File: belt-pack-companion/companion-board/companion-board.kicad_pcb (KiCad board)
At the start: 4 copper layers, 29.4 x 47.2 mm, 58 parts, among them J1 Conn_01x18_Socket, J2 Conn_01x18_Socket, J4 Conn_01x03_Pin, U1 TLV320AIC3204, X1 YC24.576MUBCE2O

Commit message: Routing Progress
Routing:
- net LED_Red: track 0.00 -> 32.5 mm, vias 0 -> 1
- net SD_DETECT: track 1.31 -> 29.5 mm, vias 0 -> 1
- net Button_1: track 0.00 -> 24.5 mm, vias 0 -> 1
- net Net-(U1-IN2_R): track 0.00 -> 23.0 mm, vias 0 -> 2
- net Net-(U1-IN2_L): track 0.00 -> 22.4 mm, vias 0 -> 2
- net Button_2: track 0.00 -> 19.9 mm, vias 0 -> 1
- net LINE_IN_L: track 0.00 -> 4.88 mm
- net Net-(D1-Pad2): track 0.00 -> 1.18 mm
- net +3.3V: track 32.7 -> 33.8 mm, vias 9 -> 11
- net GND: vias 5 -> 6

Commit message: Routing complete
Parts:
- moved JP4 2.37 mm to (133.3, 73.4), turned to 0 degrees
- moved C1 0.06 mm to (129.2, 60.0)
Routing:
- net SD_DAT0: track 1.32 -> 37.7 mm, vias 0 -> 4
- net SD_DAT1: track 1.32 -> 37.7 mm, vias 0 -> 3
- net SD_CMD: track 1.32 -> 35.0 mm, vias 0 -> 2
- net MIC: track 18.1 -> 42.5 mm, vias 1 -> 2
- net SD_CLK: track 0.00 -> 21.6 mm, vias 0 -> 1
- net CODEC_RESET: track 1.07 -> 21.7 mm, vias 0 -> 1
- net I^{2}S_SPK_DATA: track 0.00 -> 18.7 mm, vias 0 -> 2
- net I^{2}S_WCLK: track 0.00 -> 18.4 mm, vias 0 -> 1
- net Button_PTT: track 1.52 -> 17.4 mm
- net I^{2}S_BCLK: track 0.00 -> 14.8 mm, vias 0 -> 1
- net I^{2}S_MIC_DATA: track 0.00 -> 14.4 mm
- net SD_DAT2: track 1.31 -> 13.4 mm, vias 0 -> 1
- net SD_DAT3: track 1.31 -> 13.3 mm
- net GND: track 7.30 -> 16.5 mm, vias 6 -> 37
- net LINE_IN_L: track 4.88 -> 12.4 mm
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
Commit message: Theoretically Finished Rev.1 of companion board
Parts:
- moved JP3 2.38 mm to (127.8, 71.5)
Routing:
- net GND: track 16.5 -> 19.6 mm, vias 37 -> 40
- net Net-(JP3-A): track 1.83 -> 3.72 mm
- net I^{2}S_SPK_DATA: track 18.7 -> 19.6 mm

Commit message: Incremented revision number to 1.1
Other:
- board text added: "Heltec WiFi LoRa 32 v3 Companion Board Rev 1.1"
- board text added: "Heltec v3 Companion Rev 1.1"
- board text removed: "Heltec WiFi LoRa 32 v3 Companion Board Rev.1"
- board text removed: "Heltec v3 Companion Rev.1"
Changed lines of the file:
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@@
 		)
 	)
-	(gr_text "Heltec v3\nCompanion\nRev.1"
+	(gr_text "Heltec v3\nCompanion\nRev 1.1"
 		(at 134.3 82.55 90)
 		(layer "F.SilkS")
@@
 		)
 	)
-	(gr_text "Heltec WiFi LoRa 32 v3\nCompanion Board\nRev.1"
+	(gr_text "Heltec WiFi LoRa 32 v3\nCompanion Board\nRev 1.1"
 		(at 123.318262 81.009202 0)
 		(layer "B.SilkS")
@@
 	)
 	(segment
-		(start 122.55 79.9076)
+		(start 121.65 79.9076)
 		(end 126.37627 79.9076)
 		(width 0.2)
@@
 	)
 	(via
-		(at 122.55 79.9076)
+		(at 121.65 79.9076)
 		(size 0.6)
 		(drill 0.3)
@@
 	)
 	(segment
-		(start 122.55 79.9076)
+		(start 121.65 79.9076)
 		(end 114.1604 79.9076)
 		(width 0.2)

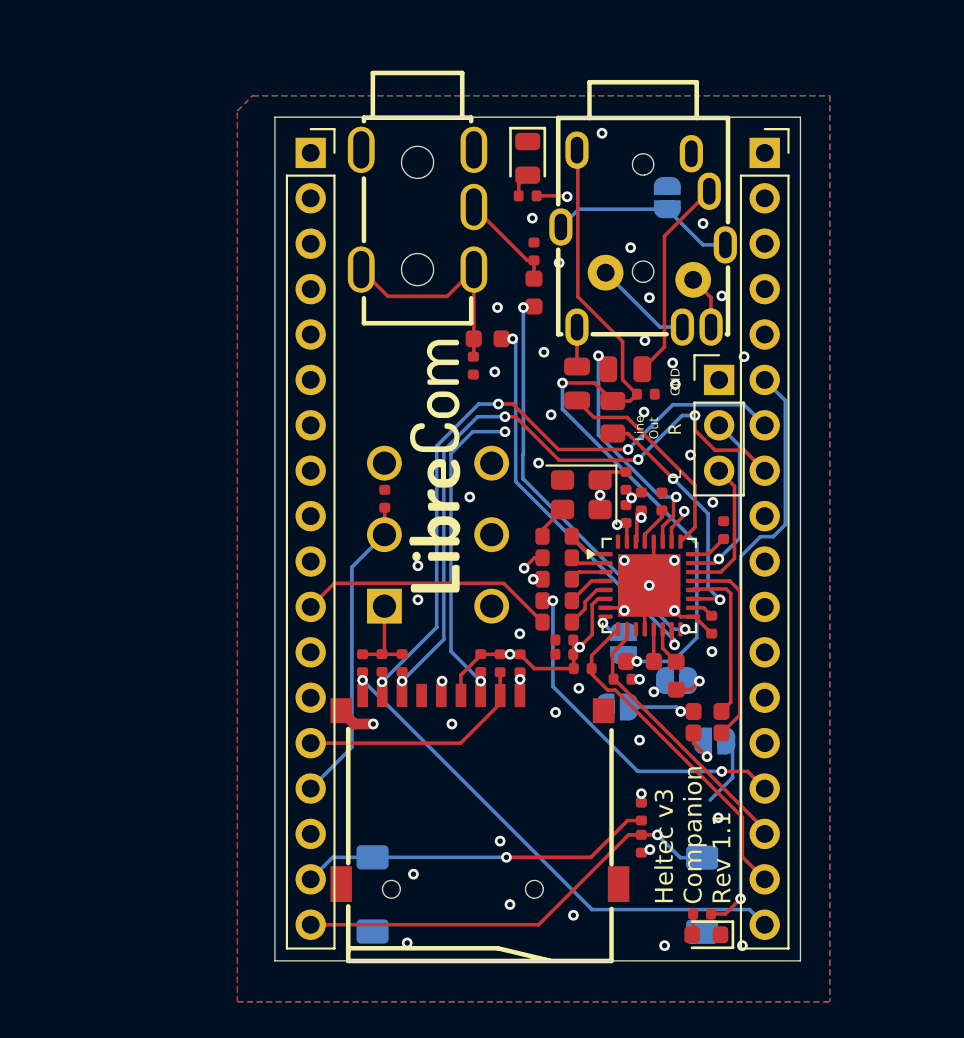
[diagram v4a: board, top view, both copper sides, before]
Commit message: PCB & Schematic Edits
Increased PCB size and brought PTT Button onto the same side as the audio jacks. Re-positioned Silkscreen text. Added mounting holes.
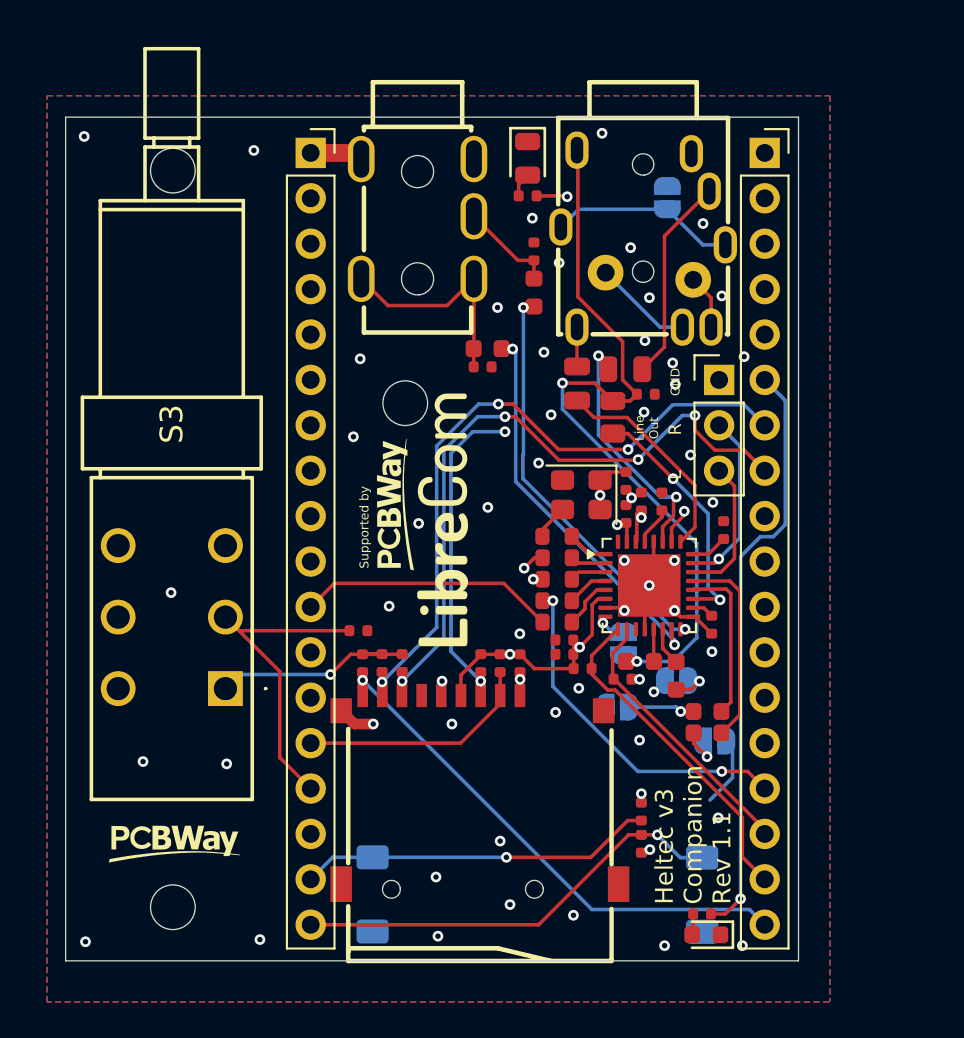
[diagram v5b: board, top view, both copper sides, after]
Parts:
- added H1: MountingHole, MountingHole:MountingHole_2.5mm, F.Cu at (116.0, 54.5)
- added H2: MountingHole, MountingHole:MountingHole_2.5mm, F.Cu at (103.0, 82.7)
- added H3: MountingHole, MountingHole:MountingHole_2.5mm, F.Cu at (103.0, 41.5)
- S3: moved to F.Cu
- moved S3 10.0 mm to (105.9, 70.5)
- moved R24 7.53 mm to (113.4, 67.2), turned to 0 degrees
- moved C10 0.55 mm to (120.6, 51.5)
- moved R32 0.52 mm to (120.3, 52.5), turned to 0 degrees
- moved J3 0.52 mm to (116.7, 44.2)
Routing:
- net +3.3V: track 37.1 -> 43.9 mm, vias 12 -> 13
- net GND: track 19.6 -> 22.5 mm, vias 40 -> 48
- net Button_PTT: track 17.4 -> 18.8 mm
- net Net-(U1-IN2_L): track 22.4 -> 21.2 mm
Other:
- board size 29.4 x 47.2 mm -> 41 x 47.2 mm
- board text added: "Button1"
- board text added: "Button2"
- board text added: "Heltec WiFi LoRa 32 v3 Companion Board Rev 1.2"
- board text removed: "Heltec WiFi LoRa 32 v3 Companion Board Rev 1.1"

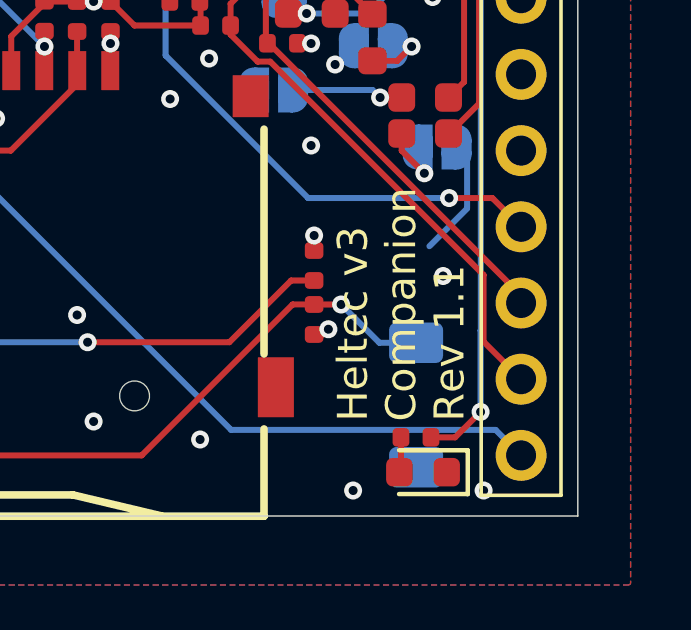
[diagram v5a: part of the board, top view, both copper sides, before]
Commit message: PCB edits
silkscreen was wrong
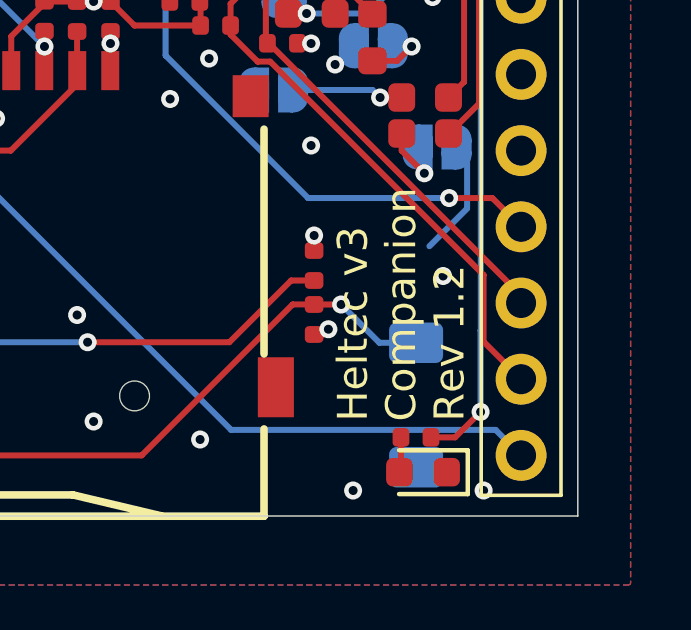
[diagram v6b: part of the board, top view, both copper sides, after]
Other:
- board text added: "Heltec v3 Companion Rev 1.2"
- board text removed: "Heltec v3 Companion Rev 1.1"
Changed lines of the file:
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@@
 		)
 	)
-	(gr_text "Heltec v3\nCompanion\nRev 1.1"
+	(gr_text "Heltec v3\nCompanion\nRev 1.2"
 		(at 134.3 82.55 90)
 		(layer "F.SilkS")

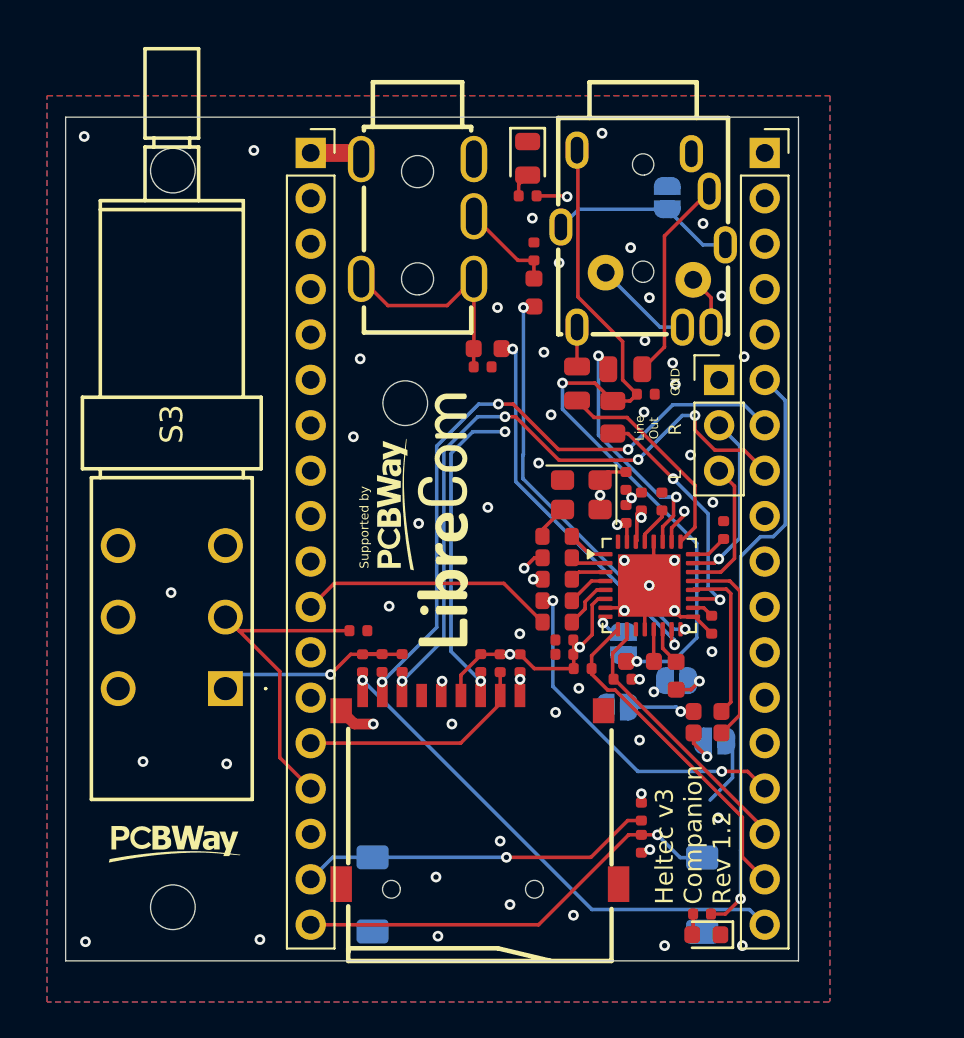
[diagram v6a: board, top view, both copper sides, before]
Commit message: schematic & pcb edits
added 33Ω resistor on SD_CLK line. Silkscreen edits.
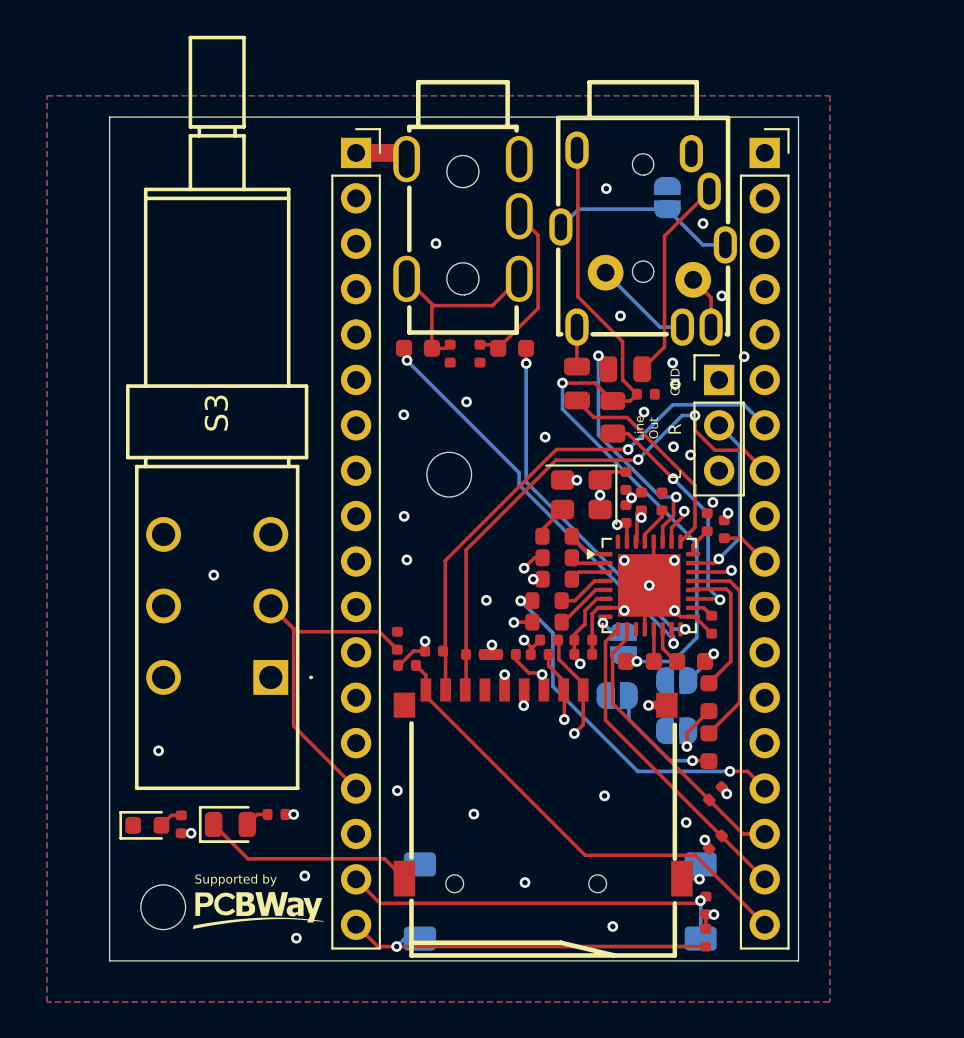
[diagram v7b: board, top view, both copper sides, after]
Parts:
- removed H3: MountingHole, MountingHole:MountingHole_2.5mm
- added R8: 33Ω, PCM_JLCPCB:R_0402, F.Cu at (133.8, 61.5)
- moved D4 40.8 mm to (106.2, 78.1), turned to 0 degrees
- moved R17 37.3 mm to (108.8, 77.5)
- moved D1 31.9 mm to (101.6, 78.1), turned to 0 degrees
- moved R18 29.6 mm to (103.5, 78.1), turned to 90 degrees
- moved S1 18.4 mm to (132.5, 82.4), turned to 90 degrees
- moved S2 15.8 mm to (116.8, 82.4), turned to 90 degrees
- moved R7 12.2 mm to (133.3, 79.1), turned to -135 degrees
- moved R14 8.25 mm to (133.3, 76.3), turned to -135 degrees
- moved R33 6.47 mm to (120.2, 51.7), turned to -90 degrees
- moved R15 6.37 mm to (132.8, 84.4), turned to 90 degrees
- moved R16 6.37 mm to (132.8, 82.6), turned to -90 degrees
- moved JP4 6.01 mm to (127.8, 70.9), turned to 180 degrees
- moved H1 4.70 mm to (118.5, 58.5)
- moved R29 4.10 mm to (119.9, 68.6), turned to 180 degrees
- moved C10 3.90 mm to (116.7, 51.4), turned to 0 degrees
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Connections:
- J1 pad 10: SD_CLK -> Net-(J1-Pin_10)
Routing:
- net LED_Green: track 16.5 -> 40.7 mm
- net LED_Red: track 33.0 -> 56.5 mm
- net GND: track 22.5 -> 36.9 mm, vias 48 -> 33
- net SD_CMD: track 35.0 -> 23.0 mm, vias 2 -> 1
- net SD_DAT1: track 37.7 -> 29.2 mm, vias 3 -> 1
- net SD_DAT0: track 37.7 -> 29.4 mm, vias 4 -> 2
- net SD_DAT2: track 13.4 -> 19.1 mm
- net LINE_IN_R: track 5.40 -> 9.85 mm
- net I^{2}S_MIC_DATA: track 14.4 -> 10.2 mm, vias 0 -> 1
- net Net-(JP4-A): track 2.61 -> 6.78 mm
- net SD_CLK: track 21.6 -> 17.6 mm, vias 1 -> 2
- net +3.3V: track 43.9 -> 40.1 mm, vias 13 -> 15
- net SD_DETECT: track 29.5 -> 26.2 mm, vias 1 -> 0
- net Net-(U1-IN2_R): track 23.0 -> 20.0 mm
- net Button_1: track 24.5 -> 21.6 mm
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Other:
- board size 41 x 47.2 mm -> 38.5 x 47.2 mm
- board text added: "Button 1"
- board text added: "Button 2"
- board text removed: "Button1"
- board text removed: "Button2"
- board text removed: "Heltec v3 Companion Rev 1.2"
